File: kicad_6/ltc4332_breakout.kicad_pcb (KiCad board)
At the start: 2 copper layers, 19.1 x 39.4 mm, 31 parts, among them J1 Conn_01x10, J2 Conn_01x06, U1 LTC4332

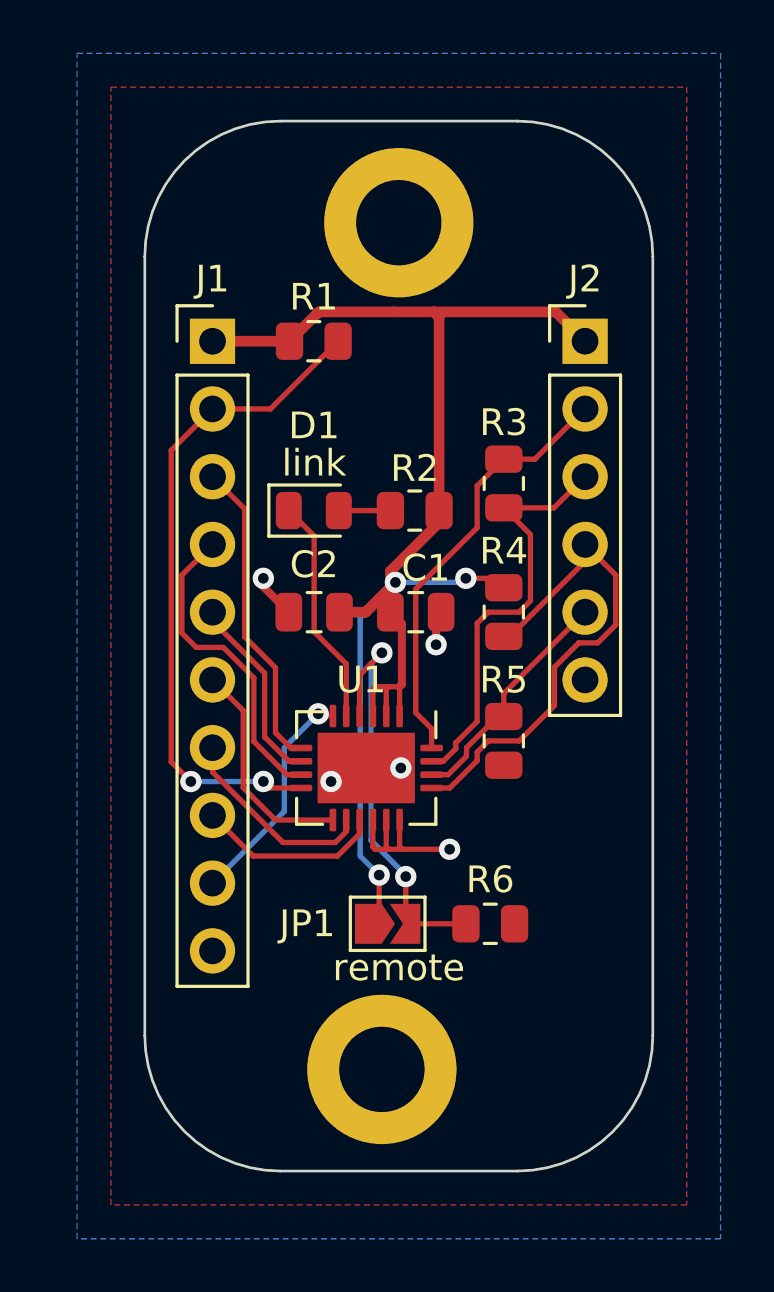
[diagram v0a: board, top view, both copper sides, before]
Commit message: Move mounting hole, minor pcb tweaks
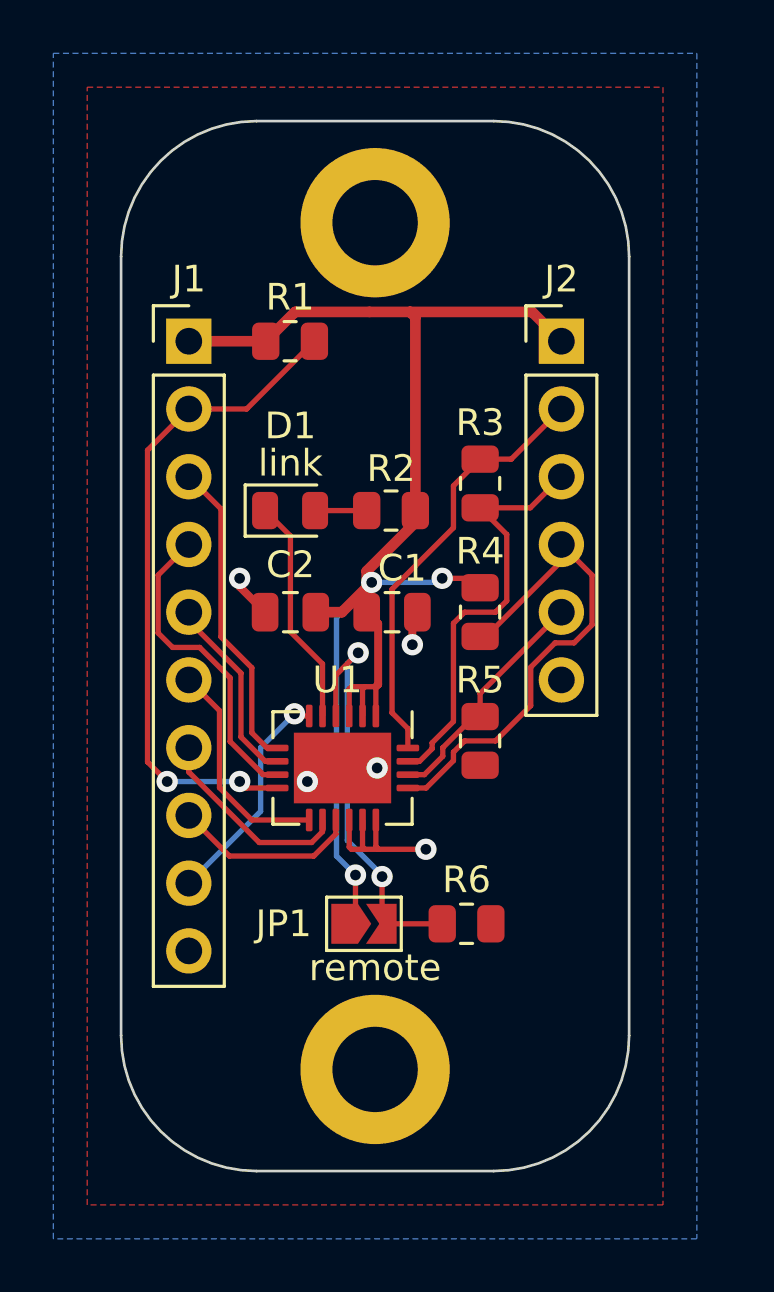
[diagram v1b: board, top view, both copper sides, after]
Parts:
- moved kibuzzard-62B2249D 2.10 mm to (152.8, 111.8)
- moved D1 0.89 mm to (144.1, 97.2)
- moved JP1 0.89 mm to (146.9, 112.6)
- moved R1 0.89 mm to (144.1, 90.8)
- moved R2 0.89 mm to (147.9, 97.2)
- moved R6 0.89 mm to (150.7, 112.6)
- moved REF** 0.89 mm to (147.3, 86.4)
- moved U1 0.89 mm to (146.1, 106.8)
- moved kibuzzard-62B219C1 0.89 mm to (150.4, 103.5)
- moved kibuzzard-62B219C1 0.89 mm to (144.3, 113.7)
- moved kibuzzard-62B22951 0.89 mm to (143.9, 93.3)
- moved kibuzzard-62B2297F 0.89 mm to (144.0, 95.9)
- moved kibuzzard-62B229AC 0.89 mm to (144.4, 98.4)
- moved kibuzzard-62B229C0 0.89 mm to (144.4, 101.0)
- moved kibuzzard-62B229D7 0.89 mm to (144.0, 103.5)
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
